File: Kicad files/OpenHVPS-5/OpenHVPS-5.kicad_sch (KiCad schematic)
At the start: 77 parts, among them J1 Conn_01x03_Male, Q1 FQT7N10, Q2 BC846A, Q3 MMDT3906, U1 MAX6008AEUR+T, U2 74HC14, U3 MAX4162, U4 CD14538BM

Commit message: Updated the board to V1.1.
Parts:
- removed TP7: TestPoint, TestPoint:TestPoint_Pad_1.5x1.5mm, symbol Connector:TestPoint
- added two_pinheader1: Conn_01x03_Male, Connector_PinHeader_2.54mm:PinHeader_1x02_P2.54mm_Vertical, symbol Connector:Conn_01x02_Male
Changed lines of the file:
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@@
     (stroke (width 0) (type solid) (color 0 0 0 0))
   )
-  (wire (pts (xy 250.19 99.695) (xy 250.19 106.68))
-    (stroke (width 0) (type solid) (color 0 0 0 0))
-  )
   (wire (pts (xy 250.19 99.695) (xy 254 99.695))
-    (stroke (width 0) (type solid) (color 0 0 0 0))
-  )
-  (wire (pts (xy 250.19 106.68) (xy 251.46 106.68))
     (stroke (width 0) (type solid) (color 0 0 0 0))
   )
@@
     (pin "1")
   )
-  (symbol (lib_id "Connector:TestPoint") (at 251.46 106.68 270) (unit 1)
-    (in_bom no) (on_board yes)
-    (property "Reference" "TP7" (id 0) (at 256.356 106.807 90)
-      (effects (font (size 1.27 1.27)) (justify left))
-    )
-    (property "Value" "TestPoint" (id 1) (at 252.1522 108.0771 0)
-      (effects (font (size 1.27 1.27)) (justify left) hide)
-    )
-    (property "Footprint" "TestPoint:TestPoint_Pad_1.5x1.5mm" (id 2) (at 251.46 111.76 0)
-      (effects (font (size 1.27 1.27)) hide)
-    )
-    (property "Datasheet" "~" (id 3) (at 251.46 111.76 0)
-      (effects (font (size 1.27 1.27)) hide)
-    )
-    (pin "1")
-  )
   (symbol (lib_id "Connector:TestPoint") (at 257.81 131.445 0) (unit 1)
     (in_bom no) (on_board yes)
@@
     )
     (property "Datasheet" "https://www.digikey.com/en/products/detail/nexperia-usa-inc/BAS16J135/2405996" (id 3) (at 125.73 145.415 0)
+      (effects (font (size 1.27 1.27)) hide)
+    )
+    (pin "1")
+    (pin "2")
+  )
+  (symbol (lib_id "Connector:Conn_01x02_Male") (at 253.365 24.765 0) (unit 1)
+    (in_bom yes) (on_board yes)
+    (property "Reference" "two_pinheader1" (id 0) (at 252.882 30.461 0))
+    (property "Value" "Conn_01x03_Male" (id 1) (at 256.057 20.06 0)
+      (effects (font (size 1.27 1.27)) hide)
+    )
+    (property "Footprint" "Connector_PinHeader_2.54mm:PinHeader_1x02_P2.54mm_Vertical" (id 2) (at 253.365 24.765 0)
+      (effects (font (size 1.27 1.27)) hide)
+    )
+    (property "Datasheet" "~" (id 3) (at 253.365 24.765 0)
       (effects (font (size 1.27 1.27)) hide)
     )
@@
       (reference "TP6") (unit 1) (value "TestPoint") (footprint "TestPoint:TestPoint_Pad_1.0x1.0mm")
     )
-    (path "/112f76a1-b928-4aa9-ad86-a760f6a8116d"
-      (reference "TP7") (unit 1) (value "TestPoint") (footprint "TestPoint:TestPoint_Pad_1.5x1.5mm")
-    )
     (path "/50eb88bf-3d65-4e85-b575-0f92e6a2605f"
       (reference "TP8") (unit 1) (value "TestPoint") (footprint "TestPoint:TestPoint_Pad_1.0x1.0mm")
@@
       (reference "U4") (unit 3) (value "CD14538BM") (footprint "Package_SO:SOIC-16_3.9x9.9mm_P1.27mm")
     )
-  )
+    (path "/26497565-dcb2-4690-827c-279081ae9bcb"
+      (reference "two_pinheader1") (unit 1) (value "Conn_01x03_Male") (footprint "Connector_PinHeader_2.54mm:PinHeader_1x02_P2.54mm_Vertical")
+    )
+  )

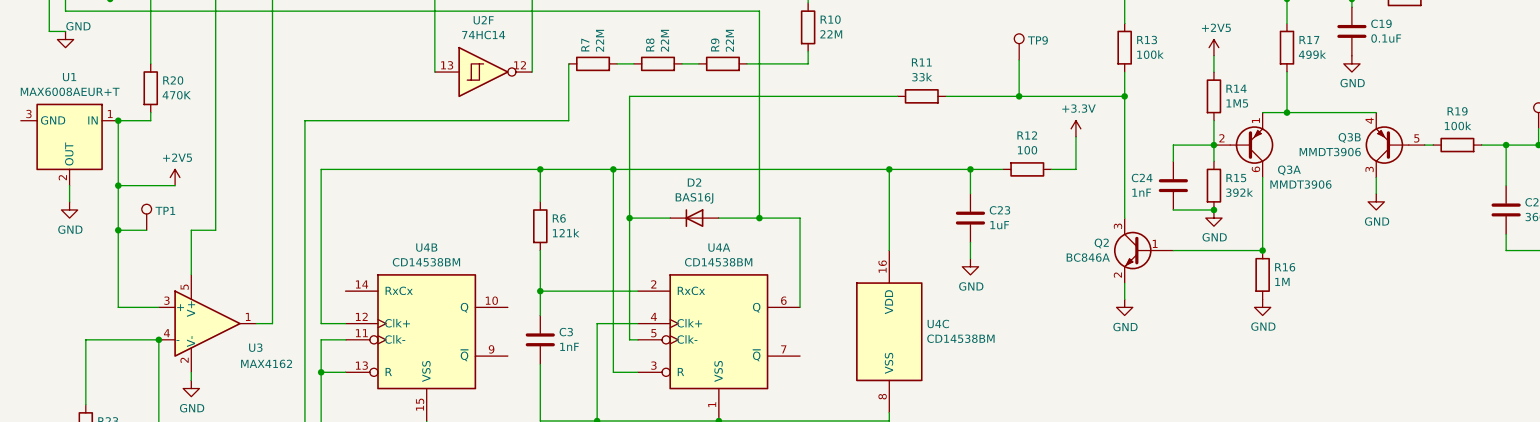
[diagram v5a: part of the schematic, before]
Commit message: Removed TP1
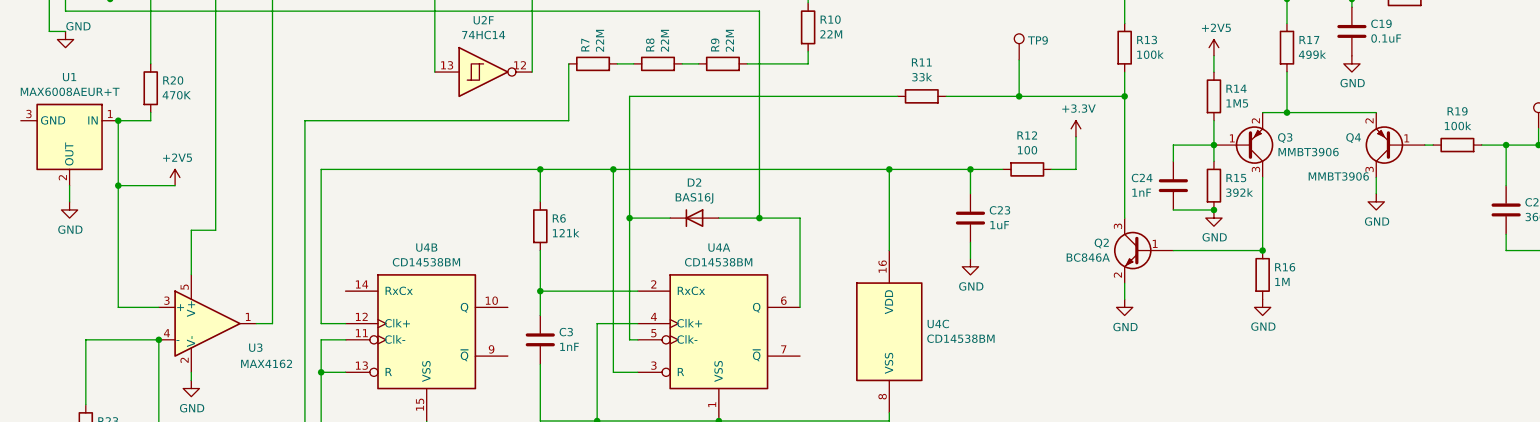
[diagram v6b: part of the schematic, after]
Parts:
- removed Q3: MMDT3906, Package_TO_SOT_SMD:SOT-363_SC-70-6, symbol Transistor_BJT:MMDT3906
- removed TP1: TestPoint, TestPoint:TestPoint_Pad_1.0x1.0mm, symbol Connector:TestPoint
- added Q3, Q4: MMBT3906, Package_TO_SOT_SMD:SOT-23, symbol Transistor_BJT:MMBT3906
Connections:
- net GND: now also Q4.3 (C)
- net at R17.2: now also Q3.2 (E), Q4.2 (E)
- net at C24.1, R14.2, R15.1: now also Q3.1 (B)
- net at Q2.1 (B), R16.1: now also Q3.3 (C)
- net at R19.1: now also Q4.1 (B)
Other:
- company: SafeCast -> SafeCast Team
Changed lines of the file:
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@@
     (title "SafePulse")
     (date "2021-02-10")
-    (rev "1.10")
-    (company "SafeCast")
+    (rev "1.11")
+    (company "SafeCast Team")
     (comment 1 "Double Sided Version")
-    (comment 2 "A. Lind & R. Oudendijk")
+    (comment 2 "contact: Allan Lind at allan@safecast.org and Rob Oudendijk at rob@safecast.org")
   )
   (junction (at 34.29 111.125) (diameter 1.016) (color 0 0 0 0))
   (junction (at 35.56 130.175) (diameter 1.016) (color 0 0 0 0))
   (junction (at 35.56 140.335) (diameter 1.016) (color 0 0 0 0))
-  (junction (at 35.56 147.32) (diameter 1.016) (color 0 0 0 0))
   (junction (at 41.275 37.465) (diameter 1.016) (color 0 0 0 0))
   (junction (at 41.91 164.465) (diameter 1.016) (color 0 0 0 0))
@@
     (stroke (width 0) (type solid) (color 0 0 0 0))
   )
-  (wire (pts (xy 35.56 140.335) (xy 35.56 147.32))
-    (stroke (width 0) (type solid) (color 0 0 0 0))
-  )
-  (wire (pts (xy 35.56 147.32) (xy 35.56 159.385))
-    (stroke (width 0) (type solid) (color 0 0 0 0))
-  )
-  (wire (pts (xy 35.56 147.32) (xy 40.005 147.32))
+  (wire (pts (xy 35.56 140.335) (xy 35.56 159.385))
     (stroke (width 0) (type solid) (color 0 0 0 0))
   )
@@
     (effects (font (size 1.27 1.27)) (justify right bottom))
   )
-  (symbol (lib_id "Connector:TestPoint") (at 40.005 147.32 0) (unit 1)
-    (in_bom no) (on_board yes)
-    (property "Reference" "TP1" (id 0) (at 41.402 144.329 0)
-      (effects (font (size 1.27 1.27)) (justify left))
-    )
-    (property "Value" "TestPoint" (id 1) (at 41.4021 146.6278 0)
-      (effects (font (size 1.27 1.27)) (justify left) hide)
-    )
-    (property "Footprint" "TestPoint:TestPoint_Pad_1.0x1.0mm" (id 2) (at 45.085 147.32 0)
-      (effects (font (size 1.27 1.27)) hide)
-    )
-    (property "Datasheet" "~" (id 3) (at 45.085 147.32 0)
-      (effects (font (size 1.27 1.27)) hide)
-    )
-    (pin "1")
-  )
   (symbol (lib_id "Connector:TestPoint") (at 69.215 103.505 0) (unit 1)
     (in_bom no) (on_board yes)
@@
     (pin "3")
   )
-  (symbol (lib_id "Transistor_BJT:MMDT3906") (at 212.09 133.985 0) (mirror x) (unit 1)
-    (in_bom yes) (on_board yes)
-    (property "Reference" "Q3" (id 0) (at 216.9414 137.8966 0)
-      (effects (font (size 1.27 1.27)) (justify left))
-    )
-    (property "Value" "MMDT3906" (id 1) (at 215.6714 140.208 0)
-      (effects (font (size 1.27 1.27)) (justify left))
-    )
-    (property "Footprint" "Package_TO_SOT_SMD:SOT-363_SC-70-6" (id 2) (at 217.17 136.525 0)
-      (effects (font (size 1.27 1.27)) hide)
-    )
-    (property "Datasheet" "https://www.digikey.com/en/products/detail/diodes-incorporated/MMDT3906-7-F/814540" (id 3) (at 212.09 133.985 0)
-      (effects (font (size 1.27 1.27)) hide)
-    )
-    (pin "1")
-    (pin "2")
-    (pin "6")
-  )
-  (symbol (lib_id "Transistor_BJT:MMDT3906") (at 234.95 133.985 180) (unit 2)
-    (in_bom yes) (on_board yes)
-    (property "Reference" "Q3" (id 0) (at 230.0986 132.8166 0)
-      (effects (font (size 1.27 1.27)) (justify left))
-    )
-    (property "Value" "MMDT3906" (id 1) (at 230.0986 135.128 0)
-      (effects (font (size 1.27 1.27)) (justify left))
-    )
-    (property "Footprint" "Package_TO_SOT_SMD:SOT-363_SC-70-6" (id 2) (at 229.87 136.525 0)
-      (effects (font (size 1.27 1.27)) hide)
-    )
-    (property "Datasheet" "https://www.digikey.com/en/products/detail/diodes-incorporated/MMDT3906-7-F/814540" (id 3) (at 234.95 133.985 0)
-      (effects (font (size 1.27 1.27)) hide)
-    )
+  (symbol (lib_id "Transistor_BJT:MMBT3906") (at 212.09 133.985 0) (mirror x) (unit 1)
+    (in_bom yes) (on_board yes)
+    (property "Reference" "Q3" (id 0) (at 216.9415 132.8356 0)
+      (effects (font (size 1.27 1.27)) (justify left))
+    )
+    (property "Value" "MMBT3906" (id 1) (at 216.9415 135.1343 0)
+      (effects (font (size 1.27 1.27)) (justify left))
+    )
+    (property "Footprint" "Package_TO_SOT_SMD:SOT-23" (id 2) (at 217.17 132.08 0)
+      (effects (font (size 1.27 1.27) italic) (justify left) hide)
+    )
+    (property "Datasheet" "https://www.fairchildsemi.com/datasheets/2N/2N3906.pdf" (id 3) (at 212.09 133.985 0)
+      (effects (font (size 1.27 1.27)) (justify left) hide)
+    )
+    (pin "1")
+    (pin "2")
     (pin "3")
-    (pin "4")
-    (pin "5")
+  )
+  (symbol (lib_id "Transistor_BJT:MMBT3906") (at 234.95 133.985 180) (unit 1)
+    (in_bom yes) (on_board yes)
+    (property "Reference" "Q4" (id 0) (at 230.0985 132.8356 0)
+      (effects (font (size 1.27 1.27)) (justify left))
+    )
+    (property "Value" "MMBT3906" (id 1) (at 231.3685 138.9443 0)
+      (effects (font (size 1.27 1.27)) (justify left))
+    )
+    (property "Footprint" "Package_TO_SOT_SMD:SOT-23" (id 2) (at 229.87 132.08 0)
+      (effects (font (size 1.27 1.27) italic) (justify left) hide)
+    )
+    (property "Datasheet" "https://www.fairchildsemi.com/datasheets/2N/2N3906.pdf" (id 3) (at 234.95 133.985 0)
+      (effects (font (size 1.27 1.27)) (justify left) hide)
+    )
+    (pin "1")
+    (pin "2")
+    (pin "3")
   )
   (symbol (lib_id "Diode:BAV99") (at 143.51 88.265 0) (unit 1)
@@
       (reference "Q2") (unit 1) (value "BC846A") (footprint "Package_TO_SOT_SMD:SOT-23")
     )
-    (path "/00000000-0000-0000-0000-0000601245d2"
-      (reference "Q3") (unit 1) (value "MMDT3906") (footprint "Package_TO_SOT_SMD:SOT-363_SC-70-6")
-    )
-    (path "/00000000-0000-0000-0000-000060124fcf"
-      (reference "Q3") (unit 2) (value "MMDT3906") (footprint "Package_TO_SOT_SMD:SOT-363_SC-70-6")
+    (path "/af22c72b-c977-455f-91df-925a662caeb1"
+      (reference "Q3") (unit 1) (value "MMBT3906") (footprint "Package_TO_SOT_SMD:SOT-23")
+    )
+    (path "/61bebb73-4eb2-47ea-98f1-32aae416543a"
+      (reference "Q4") (unit 1) (value "MMBT3906") (footprint "Package_TO_SOT_SMD:SOT-23")
     )
     (path "/00000000-0000-0000-0000-00006010b6b0"
@@
       (reference "R23") (unit 1) (value "3.16M") (footprint "Resistor_SMD:R_0805_2012Metric")
     )
-    (path "/9bc9cc82-b773-49fe-90a2-c105343e24b5"
-      (reference "TP1") (unit 1) (value "TestPoint") (footprint "TestPoint:TestPoint_Pad_1.0x1.0mm")
-    )
     (path "/10040789-70ae-4f23-b8e8-d562037e7b54"

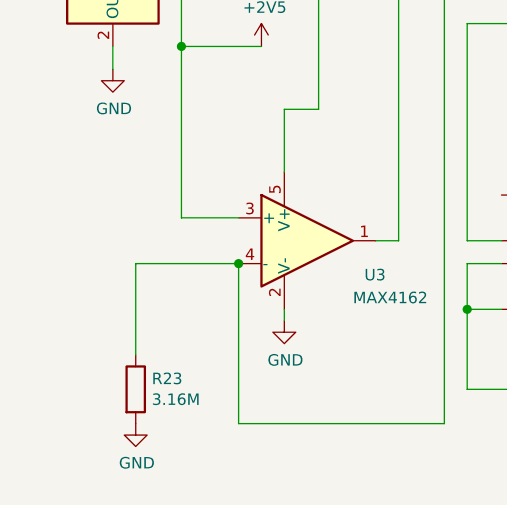
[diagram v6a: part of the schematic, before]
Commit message: Added cap for smoothing opamp
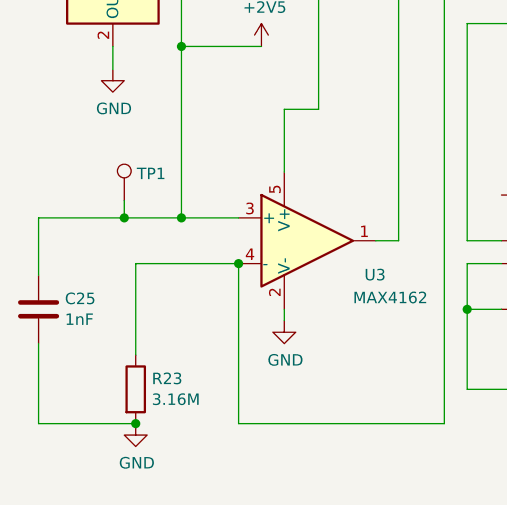
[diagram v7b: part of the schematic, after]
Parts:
- added C25: 1nF, Capacitor_SMD:C_0805_2012Metric, symbol Device:C
- added TP1: TestPoint, TestPoint:TestPoint_Pad_1.0x1.0mm, symbol Connector:TestPoint
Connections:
- net +2V5: now also C25.1, TP1.1
- net GND: now also C25.2
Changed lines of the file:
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@@
     (comment 2 "contact: Allan Lind at allan@safecast.org and Rob Oudendijk at rob@safecast.org")
   )
+  (junction (at 29.21 159.385) (diameter 1.016) (color 0 0 0 0))
+  (junction (at 30.48 182.245) (diameter 1.016) (color 0 0 0 0))
   (junction (at 34.29 111.125) (diameter 1.016) (color 0 0 0 0))
   (junction (at 35.56 130.175) (diameter 1.016) (color 0 0 0 0))
   (junction (at 35.56 140.335) (diameter 1.016) (color 0 0 0 0))
+  (junction (at 35.56 159.385) (diameter 1.016) (color 0 0 0 0))
   (junction (at 41.275 37.465) (diameter 1.016) (color 0 0 0 0))
   (junction (at 41.91 164.465) (diameter 1.016) (color 0 0 0 0))
@@
   (junction (at 263.525 150.495) (diameter 1.016) (color 0 0 0 0))
   (junction (at 278.765 105.41) (diameter 1.016) (color 0 0 0 0))
+  (wire (pts (xy 19.685 159.385) (xy 29.21 159.385))
+    (stroke (width 0) (type solid) (color 0 0 0 0))
+  )
+  (wire (pts (xy 19.685 165.735) (xy 19.685 159.385))
+    (stroke (width 0) (type solid) (color 0 0 0 0))
+  )
+  (wire (pts (xy 19.685 182.245) (xy 19.685 173.355))
+    (stroke (width 0) (type solid) (color 0 0 0 0))
+  )
   (wire (pts (xy 22.86 97.155) (xy 24.13 97.155))
     (stroke (width 0) (type solid) (color 0 0 0 0))
@@
     (stroke (width 0) (type solid) (color 0 0 0 0))
   )
+  (wire (pts (xy 29.21 157.48) (xy 29.21 159.385))
+    (stroke (width 0) (type solid) (color 0 0 0 0))
+  )
+  (wire (pts (xy 29.21 159.385) (xy 35.56 159.385))
+    (stroke (width 0) (type solid) (color 0 0 0 0))
+  )
   (wire (pts (xy 30.48 97.155) (xy 30.48 111.125))
     (stroke (width 0) (type solid) (color 0 0 0 0))
@@
   )
   (wire (pts (xy 30.48 164.465) (xy 30.48 174.625))
+    (stroke (width 0) (type solid) (color 0 0 0 0))
+  )
+  (wire (pts (xy 30.48 182.245) (xy 19.685 182.245))
     (stroke (width 0) (type solid) (color 0 0 0 0))
   )
@@
     (effects (font (size 1.27 1.27)) (justify right bottom))
   )
+  (symbol (lib_id "Connector:TestPoint") (at 29.21 157.48 0) (unit 1)
+    (in_bom no) (on_board yes)
+    (property "Reference" "TP1" (id 0) (at 30.607 154.489 0)
+      (effects (font (size 1.27 1.27)) (justify left))
+    )
+    (property "Value" "TestPoint" (id 1) (at 30.6071 156.7878 0)
+      (effects (font (size 1.27 1.27)) (justify left) hide)
+    )
+    (property "Footprint" "TestPoint:TestPoint_Pad_1.0x1.0mm" (id 2) (at 34.29 157.48 0)
+      (effects (font (size 1.27 1.27)) hide)
+    )
+    (property "Datasheet" "~" (id 3) (at 34.29 157.48 0)
+      (effects (font (size 1.27 1.27)) hide)
+    )
+    (pin "1")
+  )
   (symbol (lib_id "Connector:TestPoint") (at 69.215 103.505 0) (unit 1)
     (in_bom no) (on_board yes)
@@
       (effects (font (size 1.27 1.27)) hide)
     )
-    (property "Datasheet" "https://www.digikey.com/en/products/detail/stackpole-electronics-https://www.digikey.com/en/products/detail/stackpole-electronics-inc/RNCP0805FTD10K0/2240262" (id 3) (at 60.96 74.295 0)
+    (property "Datasheet" "https://www.digikey.com/en/products/detail/stackpole-electronics-inc/RNCP0805FTD10K0/2240262" (id 3) (at 60.96 74.295 0)
       (effects (font (size 1.27 1.27)) hide)
     )
@@
     (pin "1")
   )
+  (symbol (lib_id "Device:C") (at 19.685 169.545 0) (unit 1)
+    (in_bom yes) (on_board yes)
+    (property "Reference" "C25" (id 0) (at 22.606 168.377 0)
+      (effects (font (size 1.27 1.27)) (justify left))
+    )
+    (property "Value" "1nF" (id 1) (at 22.606 170.688 0)
+      (effects (font (size 1.27 1.27)) (justify left))
+    )
+    (property "Footprint" "Capacitor_SMD:C_0805_2012Metric" (id 2) (at 20.65 173.355 0)
+      (effects (font (size 1.27 1.27)) hide)
+    )
+    (property "Datasheet" "https://www.digikey.com/en/products/detail/avx-corporation/08055C102KAT2A/563481" (id 3) (at 19.685 169.545 0)
+      (effects (font (size 1.27 1.27)) hide)
+    )
+    (pin "1")
+    (pin "2")
+  )
   (symbol (lib_id "Device:C") (at 45.72 92.075 0) (unit 1)
     (in_bom yes) (on_board yes)
@@
       (effects (font (size 1.27 1.27)) hide)
     )
-    (property "Datasheet" "https://www.digikey.jp/product-detail/en/CL21B105KOFNNNG/1276-6471-1-ND/5958099/?itemSeq=353431115" (id 3) (at 101.6 164.465 0)
+    (property "Datasheet" "https://www.digikey.com/en/products/detail/avx-corporation/08055C102KAT2A/563481" (id 3) (at 101.6 164.465 0)
       (effects (font (size 1.27 1.27)) hide)
     )
@@
       (effects (font (size 1.27 1.27)) hide)
     )
-    (property "Datasheet" "https://www.digikey.jp/product-detail/en/CL21B105KOFNNNG/1276-6471-1-ND/5958099/?itemSeq=353431115" (id 3) (at 200.66 140.335 0)
+    (property "Datasheet" "https://www.digikey.com/en/products/detail/avx-corporation/08055C102KAT2A/563481" (id 3) (at 200.66 140.335 0)
       (effects (font (size 1.27 1.27)) hide)
     )
@@
       (effects (font (size 1.27 1.27) italic) (justify left) hide)
     )
-    (property "Datasheet" "https://www.fairchildsemi.com/datasheets/2N/2N3906.pdf" (id 3) (at 212.09 133.985 0)
+    (property "Datasheet" "https://www.digikey.com/en/products/detail/on-semiconductor/MMBT3906LT1G/919605" (id 3) (at 212.09 133.985 0)
       (effects (font (size 1.27 1.27)) (justify left) hide)
     )
@@
       (effects (font (size 1.27 1.27) italic) (justify left) hide)
     )
-    (property "Datasheet" "https://www.fairchildsemi.com/datasheets/2N/2N3906.pdf" (id 3) (at 234.95 133.985 0)
+    (property "Datasheet" "https://www.digikey.com/en/products/detail/on-semiconductor/MMBT3906LT1G/919605" (id 3) (at 234.95 133.985 0)
       (effects (font (size 1.27 1.27)) (justify left) hide)
     )
@@
       (reference "C24") (unit 1) (value "1nF") (footprint "Capacitor_SMD:C_0805_2012Metric")
     )
+    (path "/4fbbf371-3004-4032-9bf8-eb77b6b1130b"
+      (reference "C25") (unit 1) (value "1nF") (footprint "Capacitor_SMD:C_0805_2012Metric")
+    )
     (path "/00000000-0000-0000-0000-0000600ddc6a"
       (reference "D1") (unit 1) (value "BAS16J") (footprint "Diode_SMD:D_SOD-323")
@@
       (reference "R23") (unit 1) (value "3.16M") (footprint "Resistor_SMD:R_0805_2012Metric")
     )
+    (path "/a00aaed8-a3fc-4d63-a7e6-25589e061b4e"
+      (reference "TP1") (unit 1) (value "TestPoint") (footprint "TestPoint:TestPoint_Pad_1.0x1.0mm")
+    )
     (path "/10040789-70ae-4f23-b8e8-d562037e7b54"
